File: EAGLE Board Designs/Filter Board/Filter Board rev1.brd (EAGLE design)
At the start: 76.2 x 152.4 mm, 122 parts, among them J4 CONNECTOR-40__, J5 CONNECTOR-40__, U10 MAX7400, U11 MAX7400, U19 MAX7400, U20 MAX7400, U21 MAX7400, U22 MAX7400, U23 MAX7400, U24 MAX7400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

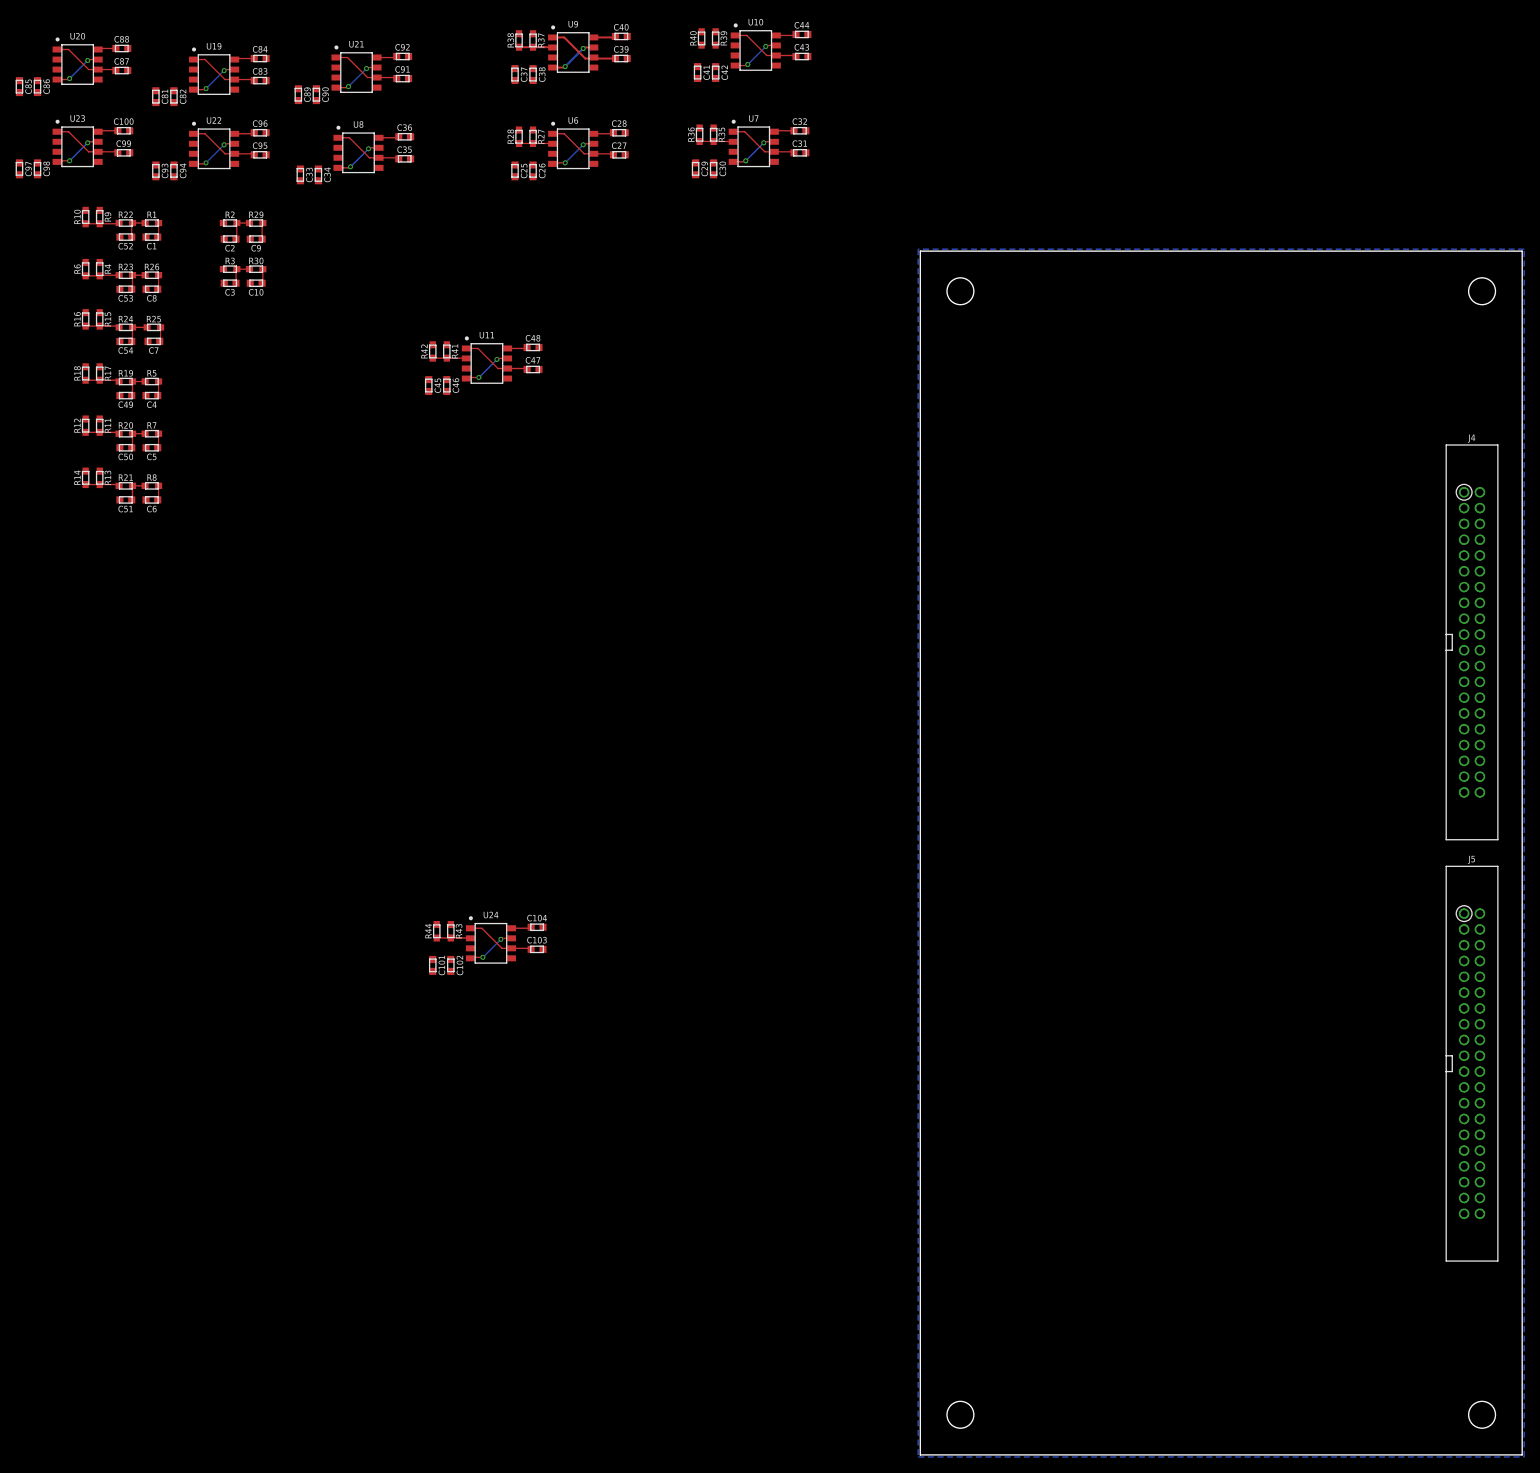
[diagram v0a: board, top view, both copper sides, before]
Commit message: Fixed width and added ground plane!
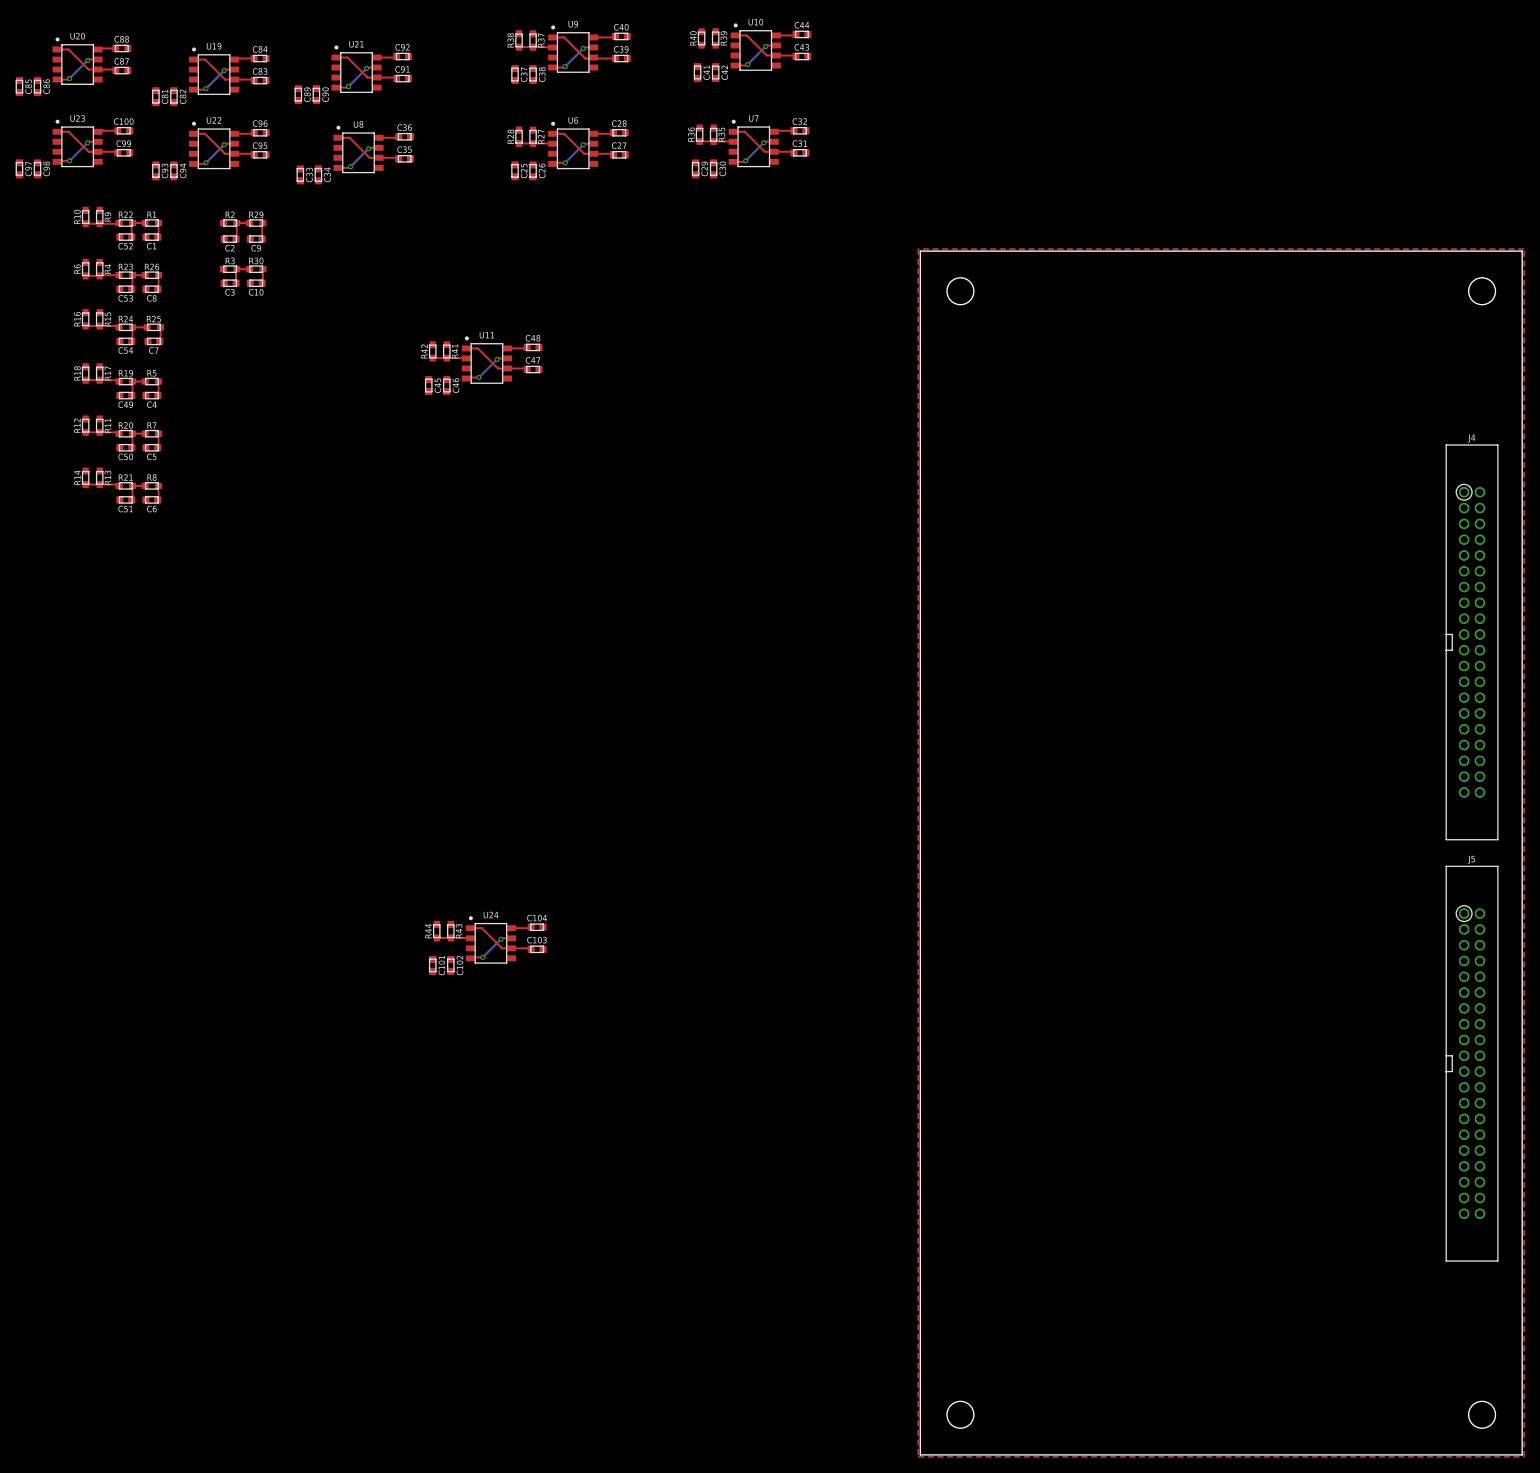
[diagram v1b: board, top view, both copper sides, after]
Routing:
- added copper zone on layer 1, net GND

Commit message: Placing things on Board!
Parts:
- moved C51 167.1 mm to (59.9, 74.7)
- moved R21 167.1 mm to (59.9, 76.5)
- moved C6 167.1 mm to (63.2, 74.7)
- moved R13 167.1 mm to (56.6, 77.5)
- moved R14 167.1 mm to (54.9, 77.5)
- moved R8 167.1 mm to (63.2, 76.5)
- moved C4 163.4 mm to (59.2, 87.1)
- moved C49 163.4 mm to (55.9, 87.1)
- moved R17 163.4 mm to (52.6, 89.9)
- moved R18 163.4 mm to (50.8, 89.9)
- moved R19 163.4 mm to (55.9, 88.9)
- moved R5 163.4 mm to (59.2, 88.9)
- moved C5 154.6 mm to (49.8, 79.8)
- moved C50 154.6 mm to (46.5, 79.8)
- moved R11 154.6 mm to (43.2, 82.5)
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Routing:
- net LOAD_RR_EXT: track 0.00 -> 83.6 mm
- net LOAD_RR: track 0.00 -> 82.2 mm
- net LOAD_RL_EXT: track 0.00 -> 64.7 mm
- net LOAD_RL: track 0.00 -> 63.3 mm
- net SPN_POT_1_EXT: track 0.00 -> 59.0 mm
- net SPN_POT_1: track 1.82 -> 52.6 mm
- net SPN_POT_2_EXT: track 0.00 -> 45.4 mm
- net LOAD_FR_EXT: track 0.00 -> 44.3 mm
- net LOAD_FR: track 0.00 -> 43.2 mm
- net SPN_POT_2: track 1.82 -> 39.4 mm
- net SPN_POT_3_EXT: track 0.00 -> 31.5 mm
- net SPN_POT_5_EXT: track 0.00 -> 30.1 mm
- net LOAD_FL: track 0.00 -> 25.6 mm
- net SPN_POT_3: track 1.82 -> 25.7 mm
- net LOAD_FL_EXT: track 0.00 -> 23.7 mm
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
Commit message: I suck at this
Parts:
- moved C97 186.5 mm to (27.9, 41.9)
- moved C100 186.5 mm to (41.1, 46.7)
- moved C98 186.5 mm to (30.2, 41.9)
- moved C99 186.5 mm to (41.1, 43.9)
- moved U23 186.5 mm to (35.3, 44.7)
- moved C10 186.3 mm to (64.0, 35.3)
- moved C3 186.3 mm to (60.7, 35.3)
- moved R3 186.3 mm to (60.7, 37.1)
- moved R30 186.3 mm to (64.0, 37.1)
- moved C2 181.7 mm to (53.1, 38.6)
- moved C9 181.7 mm to (56.4, 38.6)
- moved R2 181.7 mm to (53.1, 40.6)
- moved R29 181.7 mm to (56.4, 40.6)
- moved C85 180.5 mm to (11.7, 43.7)
- moved C86 180.5 mm to (14.0, 43.7)
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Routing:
- net SPN_POT_6: track 12.8 -> 89.5 mm
- net BRAKE_1_EXT: track 0.00 -> 66.6 mm
- net ACCEL_1_EXT: track 0.00 -> 63.8 mm
- net STEERING_1_EXT: track 0.00 -> 61.4 mm
- net BRAKE_1: track 0.00 -> 56.9 mm
- net ACCEL_1: track 0.00 -> 55.8 mm
- net SPN_POT_6_EXT: track 17.7 -> 71.9 mm
- net STEERING_1: track 0.00 -> 53.6 mm
- net BRAKE_2_EXT: track 0.00 -> 50.7 mm
- net ACCEL_2_EXT: track 0.00 -> 49.6 mm
- net STEERING_2_EXT: track 0.00 -> 46.2 mm
- net LOAD_RL: track 63.3 -> 18.4 mm
- net LOAD_RR: track 82.2 -> 39.9 mm
- net LOAD_RL_EXT: track 64.7 -> 25.7 mm
- net ACCEL_2: track 0.00 -> 36.8 mm
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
